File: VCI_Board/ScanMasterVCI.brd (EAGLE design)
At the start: 53 x 39.4 mm, 77 parts, among them IC1 XMEGA16A4A, Q13 MMBT3904, Q14 MMBT3904, Q15 MMBT3904, Q2 NDC7002N, Q3 MMBT3904, Q5 NTZD5110N, Q6 MMBT3904, Q7 ZXMP6A17G, Q8 MMBT4403, Q9 NDC7002N, U1 MAX17502FATB+, U2 SN65HVDA195-Q1, U3 MAX17502EATB+, U4 L78L08ABUTR

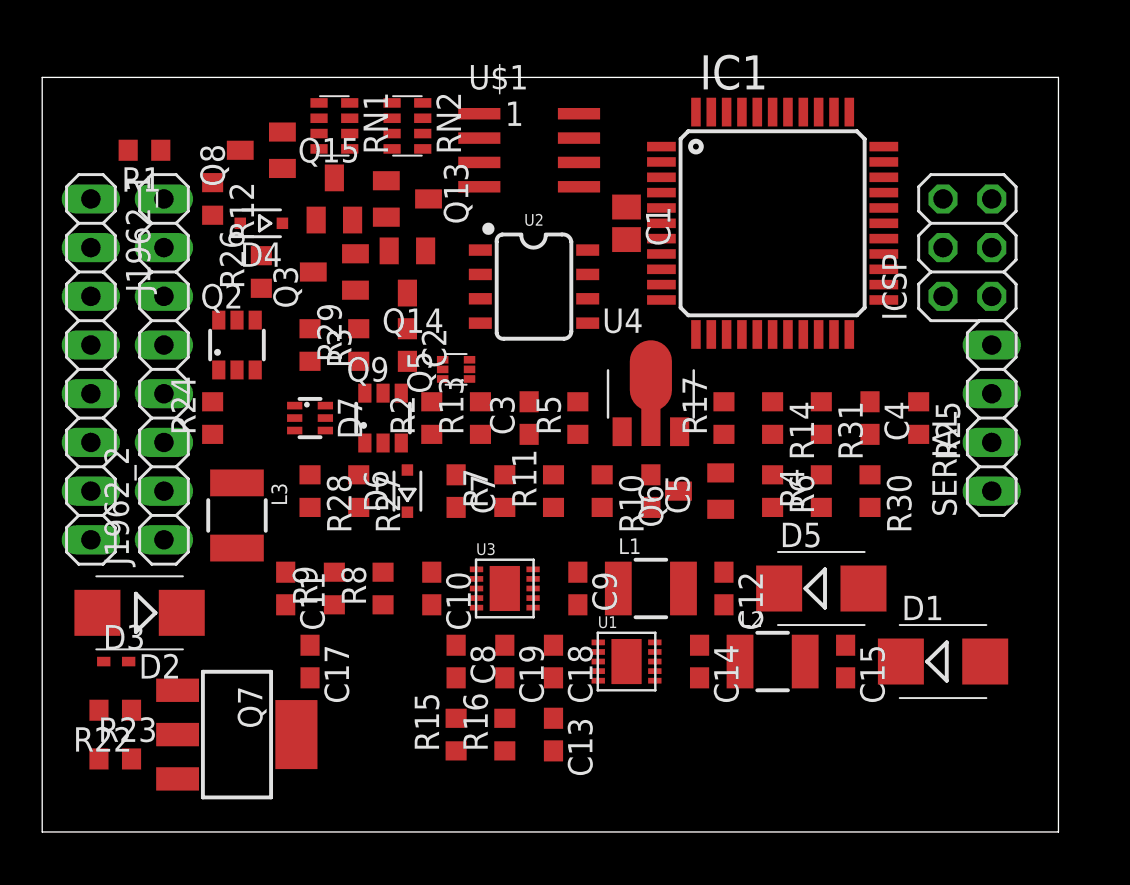
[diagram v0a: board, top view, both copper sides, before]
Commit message: Added routing. Autorouter was able to route 100%, so I went ahead and committed the board with the traces.
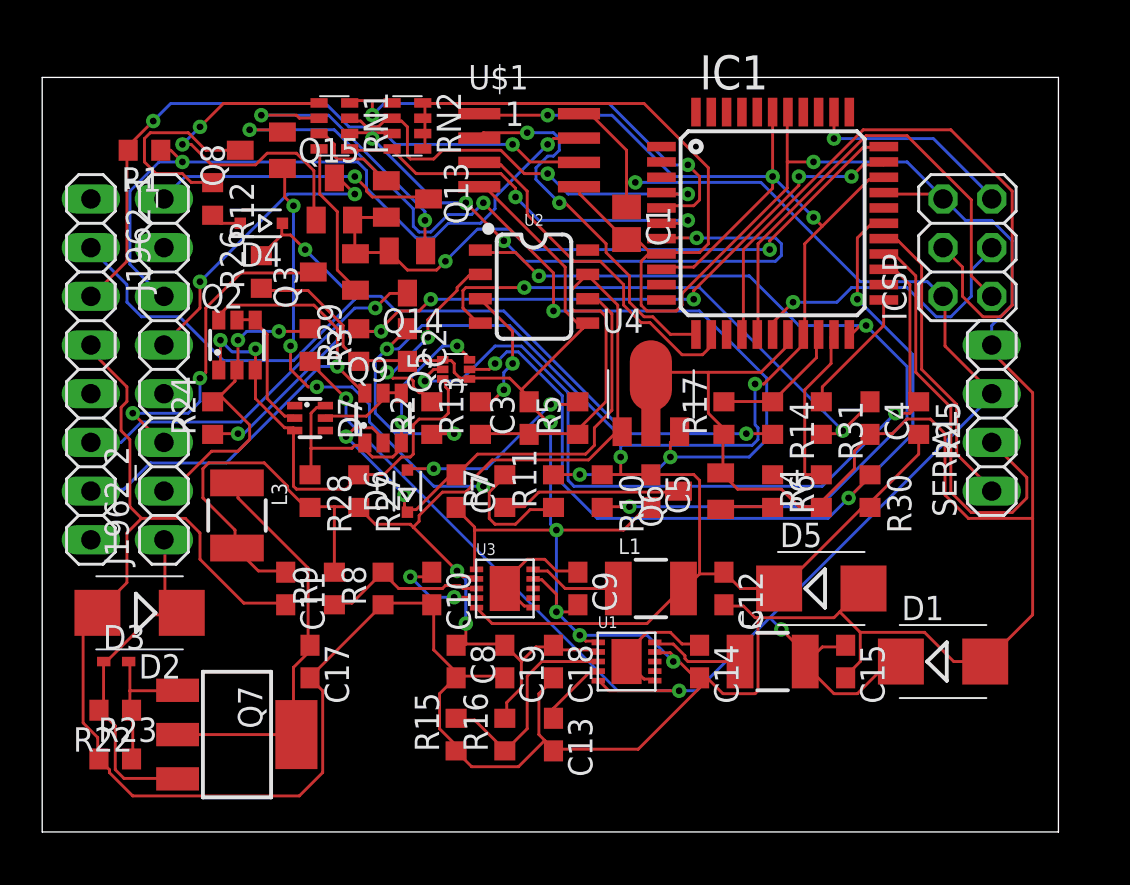
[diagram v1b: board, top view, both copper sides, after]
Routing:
- net GND: track 0.00 -> 323.9 mm, vias 0 -> 6
- net +3V3: track 0.00 -> 123.5 mm, vias 0 -> 7
- net +5V: track 0.00 -> 97.9 mm, vias 0 -> 4
- net +12V: track 0.00 -> 82.6 mm, vias 0 -> 2
- net +8V: track 0.00 -> 53.7 mm, vias 0 -> 5
- net J1962-2: track 0.00 -> 50.3 mm, vias 0 -> 2
- net ISO-K-RX: track 0.00 -> 46.5 mm, vias 0 -> 3
- net SCI-A-TX-EN: track 0.00 -> 46.4 mm, vias 0 -> 3
- net ISO-K-EN: track 0.00 -> 43.4 mm, vias 0 -> 2
- net SCI-RX: track 0.00 -> 42.9 mm, vias 0 -> 6
- net J1962-11: track 0.00 -> 36.4 mm, vias 0 -> 2
- net SCI-TX: track 0.00 -> 35.6 mm, vias 0 -> 2
- net MOSI: track 0.00 -> 34.6 mm
- net J1962-3: track 0.00 -> 34.5 mm, vias 0 -> 2
- net SCI-B-TRANS-EN: track 0.00 -> 33.7 mm, vias 0 -> 4
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
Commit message: Had to change inductors. Inductor package I was using apparently has no basis in reality. Switched it out for a standard 0603.
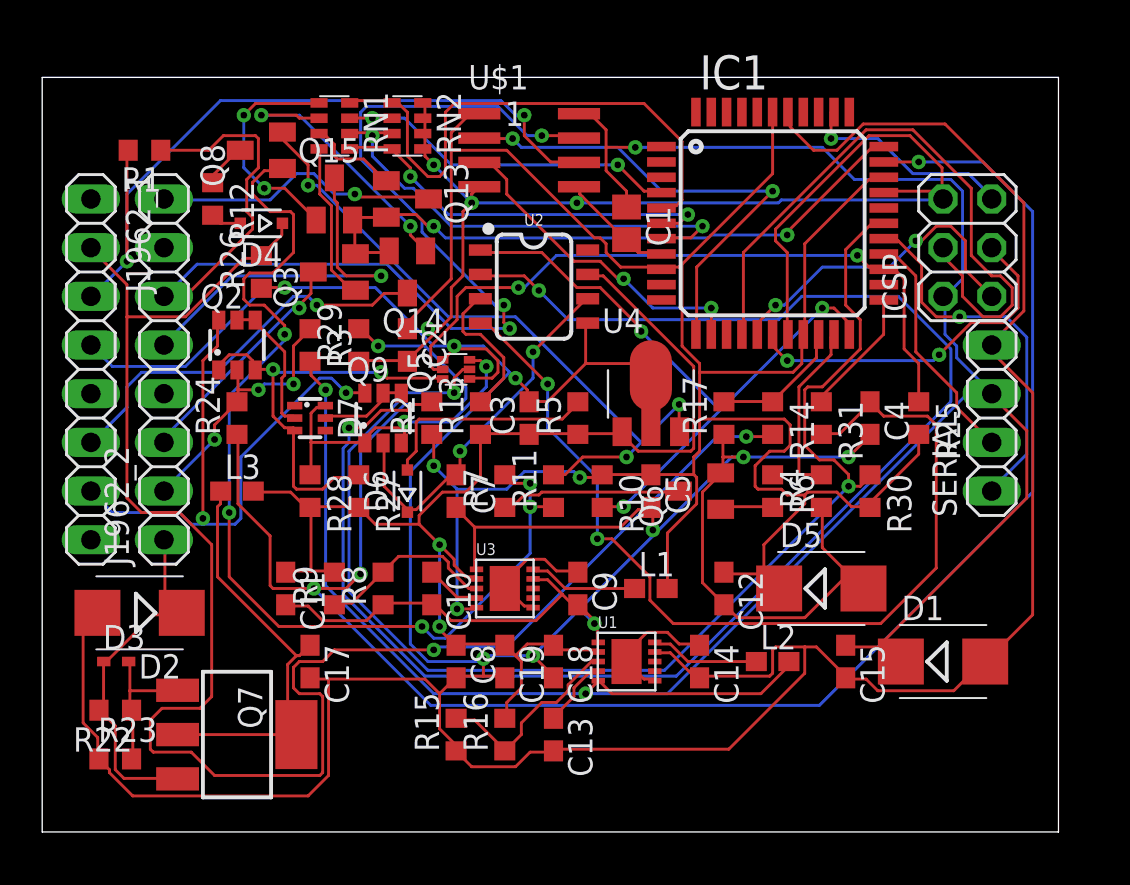
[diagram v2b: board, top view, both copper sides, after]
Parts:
- L1, L2, L3: device inductor-neosid:MS50 -> customics:L0603
- moved L3 1.27 mm to (10.2, 20.3), turned to 0 degrees
- moved R24 1.27 mm to (10.2, 24.1)
- turned L1 to 0 degrees
- turned L2 to 0 degrees
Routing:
- net N$8: track 10.7 -> 83.1 mm
- net SCI-RX: track 42.9 -> 102.4 mm, vias 6 -> 4
- net J1962-2: track 50.3 -> 89.4 mm
- net GND: track 323.9 -> 357.9 mm, vias 6 -> 13
- net +5V: track 97.9 -> 127.5 mm, vias 4 -> 3
- net J1962-11: track 36.4 -> 63.7 mm, vias 2 -> 3
- net N$28: track 30.8 -> 53.6 mm, vias 4 -> 5
- net N$10: track 28.4 -> 50.2 mm
- net SCI-A-TX-EN: track 46.4 -> 67.2 mm, vias 3 -> 2
- net +8V: track 53.7 -> 35.8 mm, vias 5 -> 3
- net +12V: track 82.6 -> 67.7 mm
- net ISO-K-RX: track 46.5 -> 34.2 mm
- net PC-RX: track 22.5 -> 12.5 mm
- net SCI-B-TRANS-EN: track 33.7 -> 24.6 mm, vias 4 -> 2
- net ISO-K: track 27.9 -> 19.5 mm
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
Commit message: It was pointed out to me that the legs of my transistor were reversed. Fixed.
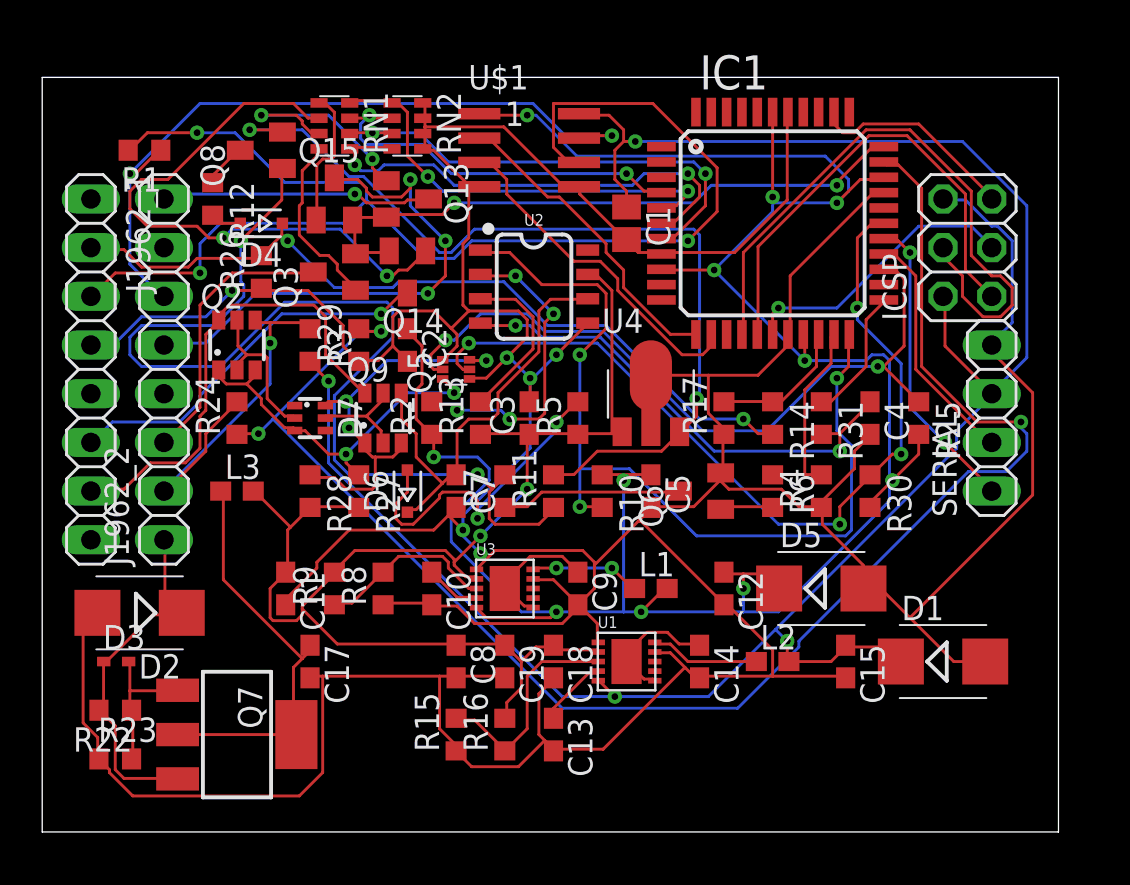
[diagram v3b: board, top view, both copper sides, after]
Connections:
- net ISO-K: now also Q9.4; no longer Q9.2
- net J1962-15: now also Q2.4; no longer Q2.2
- net N$1: now also Q2.2; no longer Q2.4
- net N$4: now also Q9.2; no longer Q9.4
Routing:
- net N$8: track 83.1 -> 16.5 mm, vias 2 -> 4
- net GND: track 357.9 -> 306.0 mm, vias 13 -> 6
- net J1962-2: track 89.4 -> 42.0 mm
- net J1962-3: track 39.6 -> 68.7 mm, vias 2 -> 3
- net J1962-11: track 63.7 -> 38.5 mm, vias 3 -> 2
- net N$10: track 50.2 -> 25.8 mm
- net SCI-A-TX-EN: track 67.2 -> 44.6 mm, vias 2 -> 4
- net SCI-RX: track 102.4 -> 82.2 mm, vias 4 -> 3
- net +5V: track 127.5 -> 108.6 mm, vias 3 -> 4
- net N$21: track 14.9 -> 30.8 mm
- net ISO-K-RX: track 34.2 -> 47.0 mm
- net +8V: track 35.8 -> 46.8 mm, vias 3 -> 2
- net CCD-RX: track 25.6 -> 16.3 mm, vias 2 -> 0
- net MISO: track 17.3 -> 25.0 mm, vias 2 -> 0
- net J1962-12: track 20.0 -> 27.1 mm, vias 1 -> 3
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
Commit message: Centered the OBD-II "header" pins on the board. Had to move a ton of stuff around to accomodate moving the OBD-II header to the center of the board, but I am now back to auto-router able to 100% route the board.
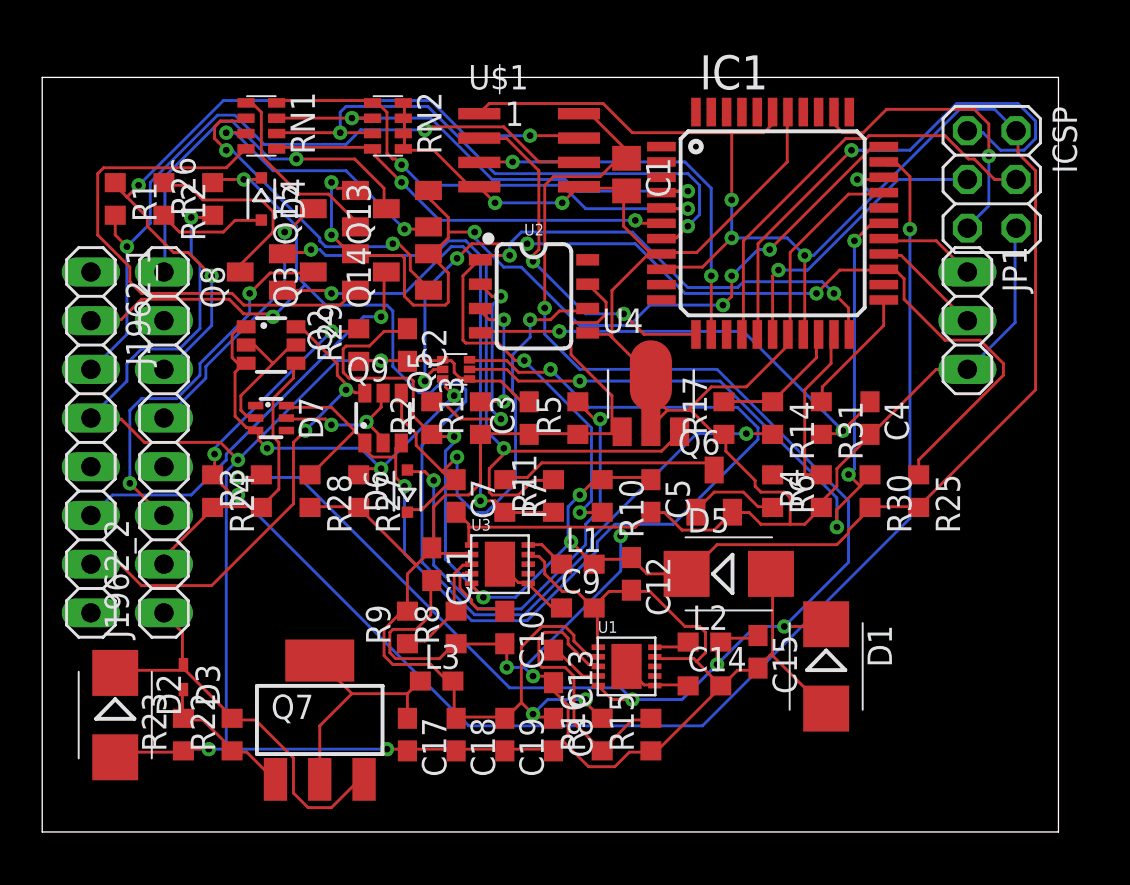
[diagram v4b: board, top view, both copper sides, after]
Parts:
- removed SERIAL: (no value), pinhead:1X04
- added JP1: (no value), pinhead:1X03
- moved L3 14.4 mm to (20.6, 10.4)
- moved R15 10.2 mm to (31.8, 7.62)
- moved R3 8.03 mm to (11.4, 20.3), turned to 90 degrees
- moved C11 7.73 mm to (20.3, 16.5)
- moved C18 6.35 mm to (21.6, 7.62)
- moved C8 6.35 mm to (26.7, 7.62)
- moved Q8 6.35 mm to (11.4, 31.8)
- moved C17 6.35 mm to (19.1, 7.62)
- moved R22 6.23 mm to (9.91, 7.62), turned to 90 degrees
- moved D1 6.10 mm to (40.9, 11.2), turned to 270 degrees
- moved D2 5.48 mm to (3.81, 8.64), turned to 270 degrees
- moved R16 5.08 mm to (29.2, 7.62)
- moved C12 4.89 mm to (30.7, 16.0)
- moved D5 4.89 mm to (35.8, 16.0)
- moved C15 4.60 mm to (37.3, 11.9)
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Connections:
- net +3V3: now also ICSP.2
- net +5V: no longer ICSP.2, SERIAL.3
- net GND: now also JP1.3; no longer SERIAL.4
- net PC-RX: now also JP1.2; no longer SERIAL.2
- net PC-TX: now also JP1.1; no longer SERIAL.1
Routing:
- net N$11: track 21.2 -> 57.9 mm, vias 3 -> 2
- net GND: track 306.0 -> 270.2 mm, vias 6 -> 10
- net J1962-3: track 68.7 -> 38.5 mm, vias 3 -> 2
- net N$28: track 55.4 -> 28.2 mm
- net J1962-2: track 42.0 -> 68.7 mm, vias 2 -> 3
- net +5V: track 108.6 -> 87.7 mm, vias 4 -> 5
- net N$23: track 9.28 -> 27.2 mm
- net SCI-TX: track 33.1 -> 49.7 mm, vias 2 -> 6
- net N$21: track 30.8 -> 17.6 mm
- net J1962-12: track 27.1 -> 14.4 mm, vias 3 -> 1
- net MOSI: track 33.5 -> 22.4 mm
- net PC-TX: track 15.9 -> 5.07 mm, vias 2 -> 0
- net ISO-K-EN: track 38.6 -> 49.1 mm, vias 2 -> 4
- net +8V: track 46.8 -> 37.7 mm
- net N$18: track 21.8 -> 12.7 mm
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
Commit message: Started organizing the board. Keeping +12V components next to each other to try and reduce vias. Same for +5v and +3V3. So far not very successful, but it's a WIP.
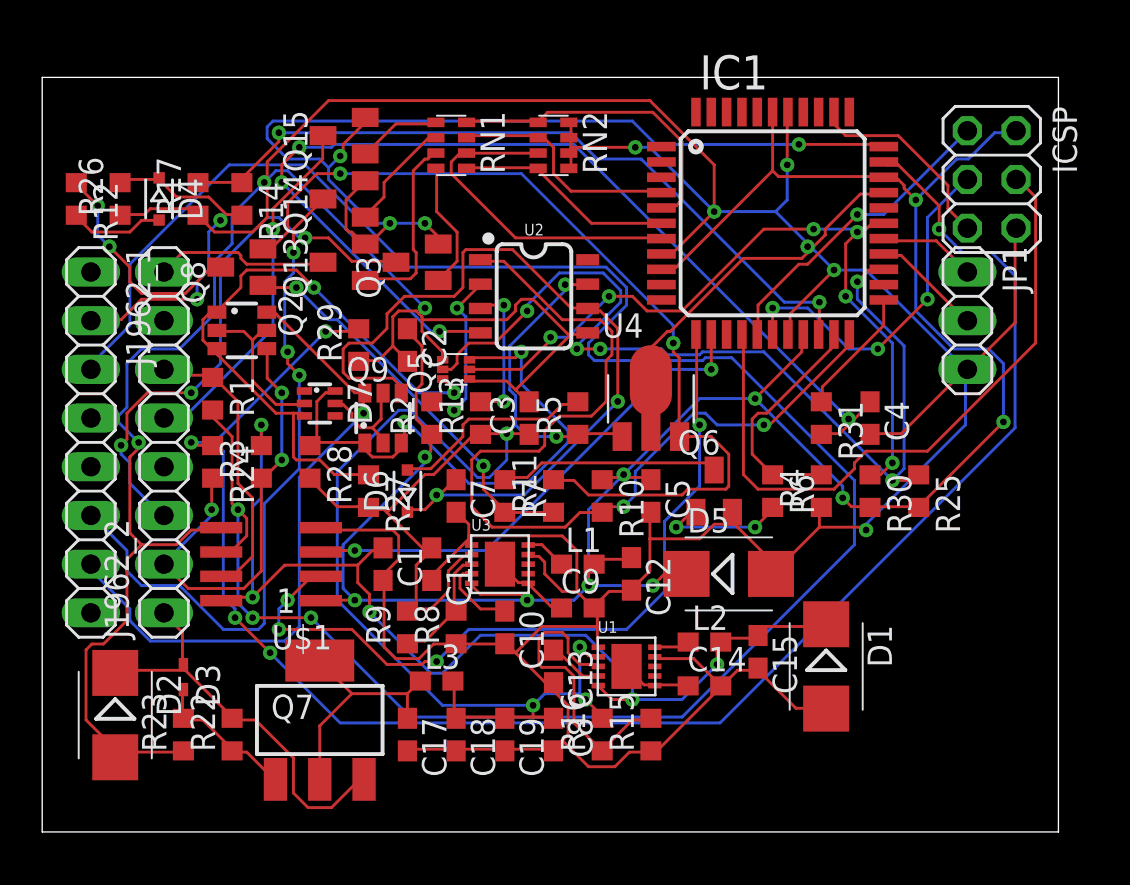
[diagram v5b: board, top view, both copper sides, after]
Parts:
- C1: device adafruit:C0805 -> adafruit:C0603
- moved R14 30.0 mm to (10.4, 35.6)
- moved R17 29.7 mm to (8.13, 35.6)
- moved U$1 25.4 mm to (11.9, 16.5), turned to 90 degrees
- moved C1 24.0 mm to (17.8, 16.5)
- moved R1 11.4 mm to (8.89, 25.4)
- moved RN1 9.96 mm to (21.3, 38.4)
- moved RN2 8.70 mm to (26.7, 38.4)
- moved D4 5.33 mm to (6.10, 35.6)
- moved Q14 5.04 mm to (15.7, 35.6)
- moved R26 4.83 mm to (4.06, 35.6)
- moved R12 4.57 mm to (1.78, 35.6)
- moved Q3 4.35 mm to (19.6, 32.3)
- moved Q13 4.33 mm to (15.7, 32.3)
- moved Q15 3.84 mm to (15.7, 38.9)
- moved D7 2.65 mm to (14.5, 24.9)
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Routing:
- net J1962-3: track 38.5 -> 113.7 mm, vias 2 -> 3
- net J1962-2: track 68.7 -> 18.3 mm, vias 3 -> 2
- net GND: track 270.2 -> 319.4 mm, vias 10 -> 9
- net +5V: track 87.7 -> 54.8 mm
- net J1850VPW-RX: track 7.04 -> 39.5 mm, vias 0 -> 2
- net N$10: track 24.4 -> 53.9 mm, vias 2 -> 4
- net N$11: track 57.9 -> 30.0 mm
- net +12V: track 66.5 -> 92.4 mm, vias 2 -> 6
- net J1962-11: track 39.9 -> 15.0 mm, vias 3 -> 0
- net CCD-RX: track 18.7 -> 40.6 mm, vias 2 -> 4
- net N$23: track 27.2 -> 6.70 mm
- net ISO-K: track 28.6 -> 43.4 mm
- net J1962-6: track 22.1 -> 36.3 mm, vias 1 -> 3
- net N$31: track 24.7 -> 10.8 mm, vias 2 -> 0
- net SCI-A-ENGINE-EN: track 25.6 -> 12.2 mm, vias 2 -> 0
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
